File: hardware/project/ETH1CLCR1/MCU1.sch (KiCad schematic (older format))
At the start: 32 parts, among them J301 Conn_02x05, J302 Conn_02x01, U301 STM32F765ZGT6, U302 24LC08B-E/MS, Y301 NX3225GD-8MHZ-STD-CRA-3

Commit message: Footprint asigment (not finished).
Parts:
- C306, C321: footprint Capacitor_SMD:C_0603_1608Metric_Pad1.05x0.95mm_HandSolder -> Capacitor_SMD:C_0805_2012Metric_Pad1.15x1.40mm_HandSolder
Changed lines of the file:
@@
 F 0 "C306" H 3265 8946 50  0000 L CNN
 F 1 "1u" H 3265 8855 50  0000 L CNN
-F 2 "Capacitor_SMD:C_0603_1608Metric_Pad1.05x0.95mm_HandSolder" H 3188 8750 50  0001 C CNN
+F 2 "Capacitor_SMD:C_0805_2012Metric_Pad1.15x1.40mm_HandSolder" H 3188 8750 50  0001 C CNN
 F 3 "~" H 3150 8900 50  0001 C CNN
 	1    3150 8900
@@
 F 0 "C321" H 8065 10746 50  0000 L CNN
 F 1 "1u" H 8065 10655 50  0000 L CNN
-F 2 "Capacitor_SMD:C_0603_1608Metric_Pad1.05x0.95mm_HandSolder" H 7988 10550 50  0001 C CNN
+F 2 "Capacitor_SMD:C_0805_2012Metric_Pad1.15x1.40mm_HandSolder" H 7988 10550 50  0001 C CNN
 F 3 "~" H 7950 10700 50  0001 C CNN
 	1    7950 10700

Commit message: Modification in schematic and PCB layout.
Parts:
- added D301: RED, LED_SMD:LED_0603_1608Metric_Pad1.05x0.95mm_HandSolder, symbol Device:LED
- added D302: GREEN, LED_SMD:LED_0603_1608Metric_Pad1.05x0.95mm_HandSolder, symbol Device:LED
- added D303: BLUE, LED_SMD:LED_0603_1608Metric_Pad1.05x0.95mm_HandSolder, symbol Device:LED
- added R306, R308: 680, Resistor_SMD:R_0603_1608Metric_Pad1.05x0.95mm_HandSolder, symbol Device:R
- added R307: 560, Resistor_SMD:R_0603_1608Metric_Pad1.05x0.95mm_HandSolder, symbol Device:R
- C306, C321: footprint Capacitor_SMD:C_0805_2012Metric_Pad1.15x1.40mm_HandSolder -> Capacitor_SMD:C_0603_1608Metric_Pad1.05x0.95mm_HandSolder
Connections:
- net +3V3: now also D301.2 (A), D302.2 (A), D303.2 (A)
- net at U301.111 (PC10,DFSDM1_CKIN5,SPI3_SCK,I2S3_CK,USART3_TX,UART4_TX,QUADSPI_BK1_IO1,SDMMC1_D2,DCMI_D8,LCD_R2,EVENTOUT): now also R306.1
- net at U301.112 (PC11,DFSDM1_DATIN5,SPI3_MISO,USART3_RX,UART4_RX,QUADSPI_BK2_NCS,SDMMC1_D3,DCMI_D4,EVENTOUT): now also R307.1
- net at U301.113 (PC12,TRACED3,SPI3_MOSI,I2S3_SD,USART3_CK,UART5_TX,SDMMC1_CK,DCMI_D9,EVENTOUT): now also R308.1
- net EEPROM_SCL renamed I2C_SCL
- net EEPROM_SDA renamed I2C_SDA
- net EEPROM_WP renamed I2C_WP
- new net: D301.1 (K), R306.2
- new net: D302.1 (K), R307.2
- new net: D303.1 (K), R308.2
- no-connect marks 87 -> 84
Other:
- moved on the sheet: C301, C302, C303, C304, C305, C306, C307, C308, C309, C310, C311, C312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

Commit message: Redesinged ADC schematic.
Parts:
- renumbered C307 to C301, C308 to C302, C301 to C303, C309 to C304, C302 to C305, C310 to C306, C303 to C307, C311 to C308, C304 to C309, C312 to C310, C306 to C311, C313 to C312, C314 to C313, C315 to C314, C316 to C315, C317 to C316, C318 to C317, C319 to C318, C320 to C319, C321 to C320, C305 to C321, J302 to J301, J301 to J302, R306 to R301, R307 to R302, R308 to R303, R305 to R304, R301 to R305, R302 to R306, R304 to R307, R303 to R308

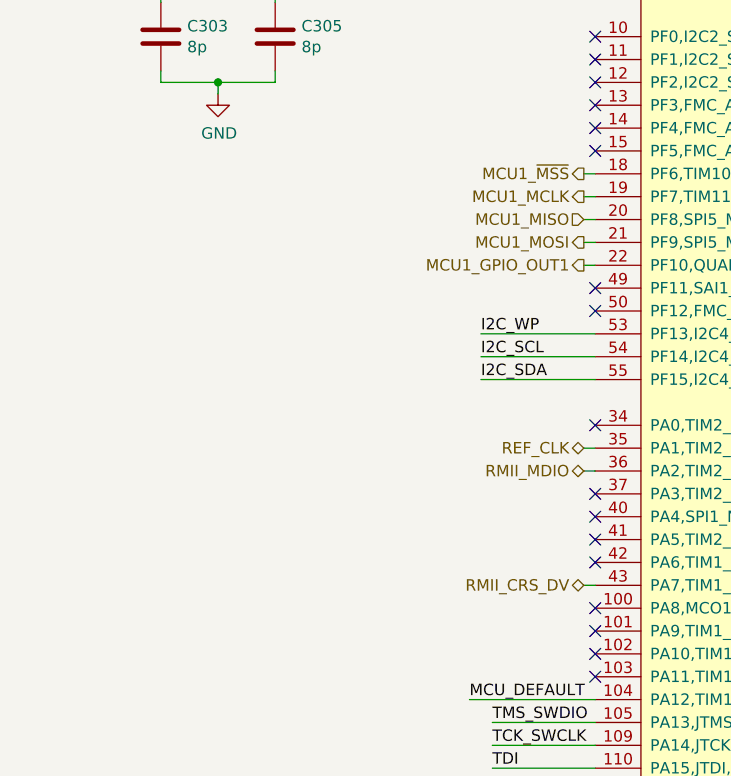
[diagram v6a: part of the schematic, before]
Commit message: Redesigned the power supply, added humidy+temp. sensor.
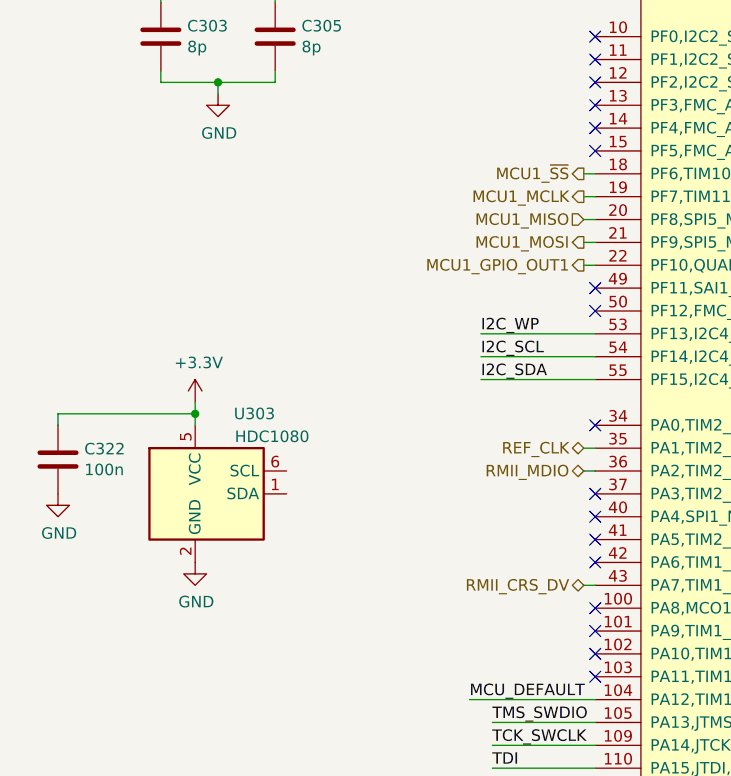
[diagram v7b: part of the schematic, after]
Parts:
- added C322: 100n, Capacitor_SMD:C_0603_1608Metric_Pad1.05x0.95mm_HandSolder, symbol Device:C
- added U303: HDC1080, Package_SON:Texas_PWSON-N6, symbol Sensor_Humidity:HDC1080
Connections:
- net +3V3: now also C322.1, U303.5 (VCC)
- net GND: now also C322.2, U303.2 (GND)
- net MCU1_~MSS renamed MCU1_~SS
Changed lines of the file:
@@
 $Descr A3 16535 11693
 encoding utf-8
-Sheet 3 16
+Sheet 3 15
 Title ""
 Date ""
@@
 	3000 2350 3050 2350
 Text HLabel 3000 2050 0    50   Output ~ 0
-MCU1_~MSS
+MCU1_~SS
 Text HLabel 3000 2250 0    50   Input ~ 0
 MCU1_MISO
@@
 Wire Wire Line
 	2050 6250 2100 6250
+$Comp
+L Sensor_Humidity:HDC1080 U303
+U 1 1 5EF9C579
+P 1400 3450
+F 0 "U303" H 1650 3800 50  0000 R CNN
+F 1 "HDC1080" H 1800 3700 50  0000 R CNN
+F 2 "Package_SON:Texas_PWSON-N6" H 1350 3200 50  0001 L CNN
+F 3 "http://www.ti.com/lit/ds/symlink/hdc1080.pdf" H 1000 3700 50  0001 C CNN
+	1    1400 3450
+	1    0    0    -1
+$EndComp
+$Comp
+L power:+3.3V #PWR0101
+U 1 1 5EF9D455
+P 1300 3050
+F 0 "#PWR0101" H 1300 2900 50  0001 C CNN
+F 1 "+3.3V" H 1315 3223 50  0000 C CNN
+F 2 "" H 1300 3050 50  0001 C CNN
+F 3 "" H 1300 3050 50  0001 C CNN
+	1    1300 3050
+	1    0    0    -1
+$EndComp
+$Comp
+L power:GND #PWR0102
+U 1 1 5EF9F2A6
+P 1300 3750
+F 0 "#PWR0102" H 1300 3500 50  0001 C CNN
+F 1 "GND" H 1305 3577 50  0000 C CNN
+F 2 "" H 1300 3750 50  0001 C CNN
+F 3 "" H 1300 3750 50  0001 C CNN
+	1    1300 3750
+	1    0    0    -1
+$EndComp
+$Comp
+L Device:C C322
+U 1 1 5EFA260C
+P 700 3300
+F 0 "C322" H 815 3346 50  0000 L CNN
+F 1 "100n" H 815 3255 50  0000 L CNN
+F 2 "Capacitor_SMD:C_0603_1608Metric_Pad1.05x0.95mm_HandSolder" H 738 3150 50  0001 C CNN
+F 3 "~" H 700 3300 50  0001 C CNN
+	1    700  3300
+	1    0    0    -1
+$EndComp
+Wire Wire Line
+	1300 3150 1300 3100
+Wire Wire Line
+	700  3150 700  3100
+Wire Wire Line
+	700  3100 1300 3100
+Connection ~ 1300 3100
+Wire Wire Line
+	1300 3100 1300 3050
+$Comp
+L power:GND #PWR0103
+U 1 1 5EFC3E57
+P 700 3450
+F 0 "#PWR0103" H 700 3200 50  0001 C CNN
+F 1 "GND" H 705 3277 50  0000 C CNN
+F 2 "" H 700 3450 50  0001 C CNN
+F 3 "" H 700 3450 50  0001 C CNN
+	1    700  3450
+	1    0    0    -1
+$EndComp
 $EndSCHEMATC

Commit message: PCB layout
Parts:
- added R309, R310: 4k7, Resistor_SMD:R_0603_1608Metric_Pad1.05x0.95mm_HandSolder, symbol Device:R
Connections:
- net +3V3: now also R309.1, R310.1
- net SENS_SDA: now reaches U301.10 (PF0,I2C2_SDA,FMC_A0,EVENTOUT)
- net SENS_SDA: now also U303.1 (SDA), R310.2
- net SENS_SCL: now reaches U301.11 (PF1,I2C2_SCL,FMC_A1,EVENTOUT)
- net SENS_SCL: now also U303.6 (SCL), R309.2
- no-connect marks 84 -> 82
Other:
- moved on the sheet: C303, C305, C307, C309, C311, C321, C322, D301, D302, D303, R301, R302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
